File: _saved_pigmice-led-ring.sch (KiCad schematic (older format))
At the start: 27 parts, among them J1 Conn_01x02_Female, J2 Conn_01x03_Female

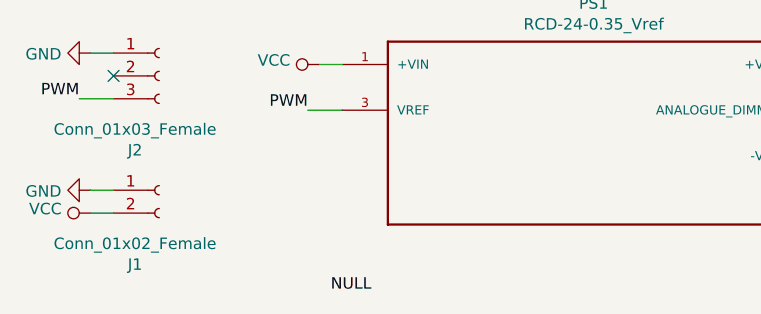
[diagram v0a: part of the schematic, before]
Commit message: rev0.2.0
* Uses an RCD-24 LED driver for constant current
* M2 mounting holes
* Powerpole, PWM connector
* Sweet graphics :sunglasses:
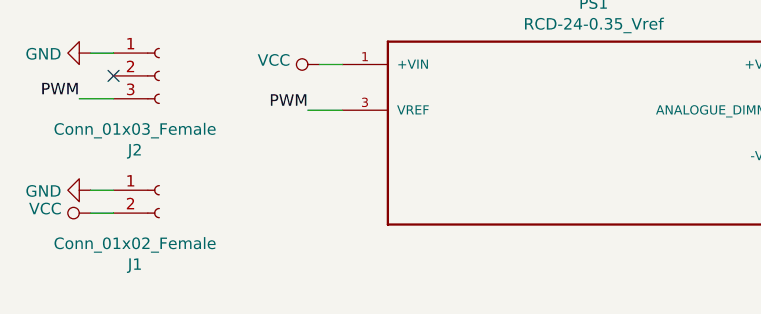
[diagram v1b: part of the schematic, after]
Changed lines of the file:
@@
 NoConn ~ 4100 2900
 NoConn ~ 900  2750
-Text Label 1850 3700 0    50   ~ 0
-NULL
 $EndSCHEMATC
